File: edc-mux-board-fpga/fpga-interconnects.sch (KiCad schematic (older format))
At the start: 7 parts

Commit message: starting to work on mezzanine board interconnections.
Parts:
- added R?: 25Ω, symbol Device:R_Small_US
- added U?: 10CL040YF484I7G, SW-Intel:FBGA-484_23.0x23.0mm_Layout22x22_P1.0mm, symbol SW-Intel:10CL040YF484I7G
- added U?: S25FL128L, symbol SW-Cypress:S25FL128L
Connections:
- wire segments 0 -> 11
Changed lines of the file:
@@
 $Descr USLedger 17000 11000
 encoding utf-8
-Sheet 22 25
+Sheet 25 28
 Title ""
 Date ""
@@
 AR Path="/5CC3E5DC/5CE97E21" Ref="U?"  Part="4"
 AR Path="/5CC6CC1A/5CD304E3/5CE97E21" Ref="U?"  Part="4"
+AR Path="/5CB2F6E3/5CE97E21" Ref="U?"  Part="4"
 F 0 "U?" H 15600 7800 50  0000 L CNN
 F 1 "10CL040YF484I7G" H 15600 7700 50  0000 L CNN
@@
 Text Label 5400 2300 0    50   ~ 0
 DIN2
+$Comp
+L SW-Intel:10CL040YF484I7G U?
+U 3 1 5CB19AD5
+P 9400 6500
+F 0 "U?" H 10100 5300 50  0000 C CNN
+F 1 "10CL040YF484I7G" H 9000 7700 50  0000 C CNN
+F 2 "SW-Intel:FBGA-484_23.0x23.0mm_Layout22x22_P1.0mm" H 12100 7400 50  0001 C CNN
+F 3 "https://www.intel.com/content/www/us/en/programmable/products/fpga/cyclone-series/cyclone-10/cyclone-10-lp/support.html" H 12100 7400 50  0001 C CNN
+	3    9400 6500
+	1    0    0    -1
+$EndComp
+$Comp
+L SW-Cypress:S25FL128L U?
+U 1 1 5CB411F7
+P 7500 6300
+F 0 "U?" H 7700 6050 50  0000 C CNN
+F 1 "S25FL128L" H 7450 6550 50  0000 C CNN
+F 2 "" H 7500 6300 50  0001 C CNN
+F 3 "https://www.cypress.com/file/316171/download" H 7500 6300 50  0001 C CNN
+	1    7500 6300
+	-1   0    0    -1
+$EndComp
+Wire Wire Line
+	7950 6150 8050 6150
+Wire Wire Line
+	7950 6450 8450 6450
+Wire Wire Line
+	7950 6350 8450 6350
+Wire Wire Line
+	7950 6250 8450 6250
+$Comp
+L Device:R_Small_US R?
+U 1 1 5CB55A13
+P 8150 6150
+F 0 "R?" V 7900 6150 50  0000 C CNN
+F 1 "25Ω" V 8000 6150 50  0000 C CNN
+F 2 "" H 8150 6150 50  0001 C CNN
+F 3 "~" H 8150 6150 50  0001 C CNN
+	1    8150 6150
+	0    1    1    0
+$EndComp
+Wire Wire Line
+	8250 6150 8450 6150
+Wire Wire Line
+	8450 5400 8200 5400
+Wire Wire Line
+	8200 5400 8200 5000
+Wire Wire Line
+	8450 5500 8200 5500
+Wire Wire Line
+	8200 5500 8200 5400
+Connection ~ 8200 5400
+Wire Wire Line
+	8450 5700 8200 5700
+Wire Wire Line
+	8200 5700 8200 5500
+Connection ~ 8200 5500
 $EndSCHEMATC

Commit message: Finished CODEC and MCU interconnections
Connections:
- net labels added: SCL, SDA, ~RESET
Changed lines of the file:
@@
 	8200 5700 8200 5500
 Connection ~ 8200 5500
+Text HLabel 2050 8650 0    50   Input ~ 0
+~RESET
+Text HLabel 2350 7000 0    50   Input ~ 0
+SCL
+Text HLabel 2300 7200 0    50   BiDi ~ 0
+SDA
 $EndSCHEMATC

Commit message: Finished FPGA and MCU interconnections.
Finished up interrupt wiring
Fixed a few missing connections
Annotated Schematic
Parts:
- added C320: 100nF, symbol Device:C_Small
- added D4: CONF_STATUS (GREEN), symbol Device:LED
- added D5: CRC_ERR, symbol Device:LED
- added D6: CONF_ERR (RED), symbol Device:LED
- added J5: Conn_02x05_Counter_Clockwise, symbol Connector_Generic:Conn_02x05_Counter_Clockwise
- added JP1: LED_ENABLE, symbol Jumper:Jumper_2_Open
- added R123, R129, R130: 200Ω, symbol Device:R_Small_US
- added R124, R125, R126, R127, R128, R132, R133: 10kΩ, symbol Device:R_Small_US
- added R134: 1kΩ, symbol Device:R_Small_US
- added unit 6 of U1
- added unit 5 of U1
- gave numbers to parts that had none: 3
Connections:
- net labels added: +2V5, +3V3, ATTACH_INT_OUT, BCLK10, BCLK11, BCLK12, BCLK13, BCLK14, BCLK15, BCLK4, BCLK5, BCLK6, BCLK7, BCLK8, BCLK9, CLK0_FPGA, DEV_ATT0, DEV_ATT1, DEV_ATT10, DEV_ATT11, DEV_ATT12, DEV_ATT13, DEV_ATT14, DEV_ATT15, DEV_ATT2, DEV_ATT3, DEV_ATT4, DEV_ATT5, DEV_ATT6, DEV_ATT7, DEV_ATT8, DEV_ATT9, DEV_ATT[0..15], DEV_INT0, DEV_INT1, DEV_INT10, DEV_INT11, DEV_INT12, DEV_INT13, DEV_INT14, DEV_INT15, DEV_INT2, DEV_INT3, DEV_INT4, DEV_INT5, DEV_INT6, DEV_INT7, DEV_INT8, DEV_INT9, DEV_INT[0..15], DEV_INT_OUT0, DEV_INT_OUT1, DEV_INT_OUT2, DEV_INT_OUT3, DEV_INT_OUT4, DEV_INT_OUT5, DEV_INT_OUT6, DEV_INT_OUT7, DEV_INT_OUT[0..7], DIN10, DIN11, DIN12, DIN13, DIN14, DIN15, DIN4, DIN5, DIN6, DIN7, DIN8, DIN9, DOUT10, DOUT11, DOUT12, DOUT13, DOUT14, DOUT15, DOUT4, DOUT5, DOUT6, DOUT7, DOUT8, DOUT9, GND, LED_PWR, TCK, TDI, TDO, TMS, WCLK10, WCLK11, WCLK12, WCLK13, WCLK14, WCLK15, WCLK4, WCLK5, WCLK6, WCLK7, WCLK8, WCLK9
- wire segments 11 -> 221
- no-connect marks 0 -> 203
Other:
- note added: "CONF_STATUS: On before and during configuration\nCONF_ERR: On if configuration error"
- note added: "DIN = input to CODEC = i2s_out in VHDL\nDOUT = output from CODEC = i2s_in in VHDL"
- note added: "LED Forward Voltage of 2V:\n(3.3V - 2V)/200Ω = 6.5mA"
- moved on the sheet: R131, U1C, U1D, U1G, U1H, U1I, U1J, U1K, U1L, U58

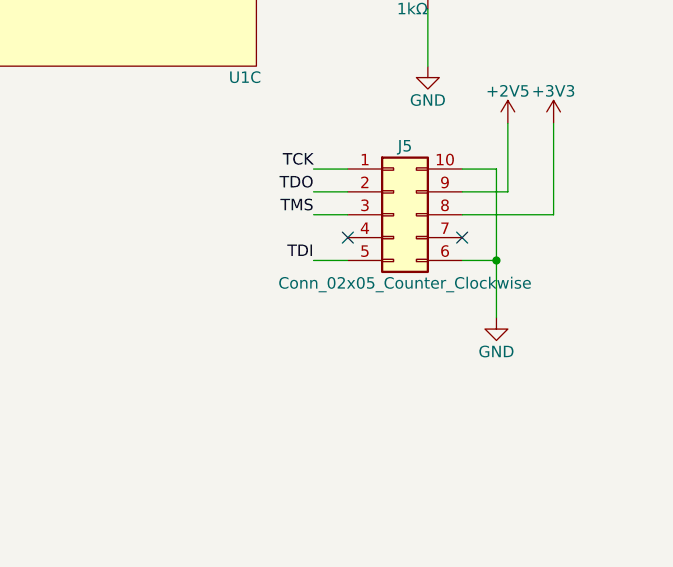
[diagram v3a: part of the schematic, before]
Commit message: assigned more footprints
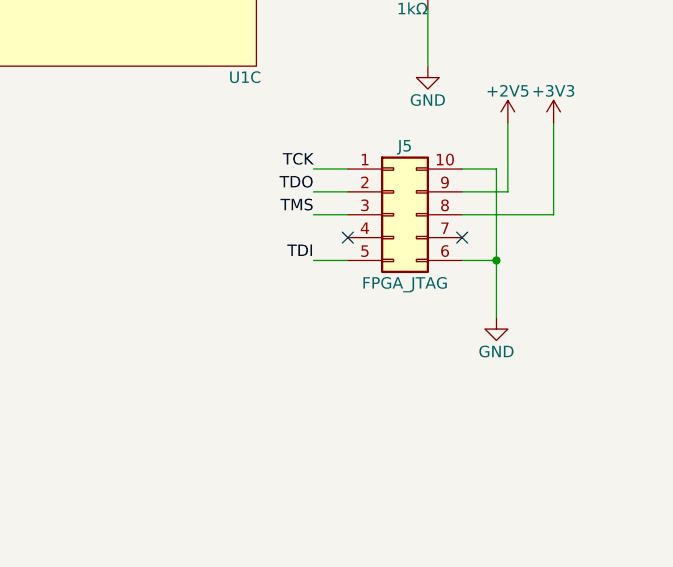
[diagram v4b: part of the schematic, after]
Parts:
- C320: footprint (none) -> Capacitor_SMD:C_0603_1608Metric; Package ID (none) -> 0603in/1608mm
- J5: value Conn_02x05_Counter_Clockwise -> FPGA_JTAG; footprint (none) -> Connector_PinHeader_1.27mm:PinHeader_2x05_P1.27mm_Vertical
- JP1: footprint (none) -> Connector_PinHeader_1.27mm:PinHeader_1x02_P1.27mm_Vertical
- R123, R124, R125, R126, R127, R128, R129, R130, R131, R132, R133, R134: footprint (none) -> Resistor_SMD:R_0402_1005Metric
- U58: footprint (none) -> Package_SON:WSON-8-1EP_6x5mm_P1.27mm_EP3.4x4mm
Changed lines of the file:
@@
 F 0 "U58" H 11750 4800 50  0000 C CNN
 F 1 "S25FL128L" H 11500 5300 50  0000 C CNN
-F 2 "" H 11550 5050 50  0001 C CNN
+F 2 "Package_SON:WSON-8-1EP_6x5mm_P1.27mm_EP3.4x4mm" H 11550 5050 50  0001 C CNN
 F 3 "https://www.cypress.com/file/316171/download" H 11550 5050 50  0001 C CNN
 	1    11550 5050
@@
 F 0 "R131" V 12000 4900 50  0000 C CNN
 F 1 "25Ω" V 12100 4900 50  0000 C CNN
-F 2 "" H 12250 4900 50  0001 C CNN
+F 2 "Resistor_SMD:R_0402_1005Metric" H 12250 4900 50  0001 C CNN
 F 3 "~" H 12250 4900 50  0001 C CNN
 	1    12250 4900
@@
 F 0 "C320" H 10850 5000 50  0000 R CNN
 F 1 "100nF" H 10850 5050 50  0000 R CNN
-F 2 "" H 10950 5050 50  0001 C CNN
+F 2 "Capacitor_SMD:C_0603_1608Metric" H 10950 5050 50  0001 C CNN
 F 3 "~" H 10950 5050 50  0001 C CNN
+F 4 "0603in/1608mm" H 0   0   50  0001 C CNN "Package ID"
 	1    10950 5050
 	1    0    0    1
@@
 F 0 "R125" V 15500 3850 50  0000 R CNN
 F 1 "10kΩ" V 15500 4200 50  0000 R CNN
-F 2 "" H 15450 3900 50  0001 C CNN
+F 2 "Resistor_SMD:R_0402_1005Metric" H 15450 3900 50  0001 C CNN
 F 3 "~" H 15450 3900 50  0001 C CNN
 	1    15450 3900
@@
 F 0 "R123" H 15150 3850 50  0000 L CNN
 F 1 "200Ω" H 15150 3900 50  0000 L CNN
-F 2 "" H 15050 3900 50  0001 C CNN
+F 2 "Resistor_SMD:R_0402_1005Metric" H 15050 3900 50  0001 C CNN
 F 3 "~" H 15050 3900 50  0001 C CNN
 	1    15050 3900
@@
 F 0 "R124" V 15350 3750 50  0000 L CNN
 F 1 "10kΩ" H 15300 4000 50  0000 L CNN
-F 2 "" H 15300 3900 50  0001 C CNN
+F 2 "Resistor_SMD:R_0402_1005Metric" H 15300 3900 50  0001 C CNN
 F 3 "~" H 15300 3900 50  0001 C CNN
 	1    15300 3900
@@
 F 0 "R126" V 15650 3850 50  0000 R CNN
 F 1 "10kΩ" V 15650 4200 50  0000 R CNN
-F 2 "" H 15600 3900 50  0001 C CNN
+F 2 "Resistor_SMD:R_0402_1005Metric" H 15600 3900 50  0001 C CNN
 F 3 "~" H 15600 3900 50  0001 C CNN
 	1    15600 3900
@@
 F 0 "R129" V 16100 3850 50  0000 R CNN
 F 1 "200Ω" V 16100 4200 50  0000 R CNN
-F 2 "" H 16050 3900 50  0001 C CNN
+F 2 "Resistor_SMD:R_0402_1005Metric" H 16050 3900 50  0001 C CNN
 F 3 "~" H 16050 3900 50  0001 C CNN
 	1    16050 3900
@@
 F 0 "JP1" V 15100 3000 50  0000 L CNN
 F 1 "LED_ENABLE" V 15050 3000 50  0000 L CNN
-F 2 "" H 15050 2900 50  0001 C CNN
+F 2 "Connector_PinHeader_1.27mm:PinHeader_1x02_P1.27mm_Vertical" H 15050 2900 50  0001 C CNN
 F 3 "~" H 15050 2900 50  0001 C CNN
 	1    15050 2900
@@
 F 0 "R134" V 15600 5900 50  0000 L CNN
 F 1 "1kΩ" H 15550 6150 50  0000 L CNN
-F 2 "" H 15550 6050 50  0001 C CNN
+F 2 "Resistor_SMD:R_0402_1005Metric" H 15550 6050 50  0001 C CNN
 F 3 "~" H 15550 6050 50  0001 C CNN
 	1    15550 6050
@@
 P 15400 7050
 F 0 "J5" H 15450 7350 50  0000 C CNN
-F 1 "Conn_02x05_Counter_Clockwise" H 15450 6750 50  0000 C CNN
-F 2 "" H 15400 7050 50  0001 C CNN
+F 1 "FPGA_JTAG" H 15450 6750 50  0000 C CNN
+F 2 "Connector_PinHeader_1.27mm:PinHeader_2x05_P1.27mm_Vertical" H 15400 7050 50  0001 C CNN
 F 3 "~" H 15400 7050 50  0001 C CNN
 	1    15400 7050
@@
 F 0 "R132" H 16100 5050 50  0000 L CNN
 F 1 "10kΩ" H 16100 5100 50  0000 L CNN
-F 2 "" H 16000 5100 50  0001 C CNN
+F 2 "Resistor_SMD:R_0402_1005Metric" H 16000 5100 50  0001 C CNN
 F 3 "~" H 16000 5100 50  0001 C CNN
 	1    16000 5100
@@
 F 0 "R133" H 16100 5050 50  0000 R CNN
 F 1 "10kΩ" H 16100 5100 50  0000 R CNN
-F 2 "" H 16200 5100 50  0001 C CNN
+F 2 "Resistor_SMD:R_0402_1005Metric" H 16200 5100 50  0001 C CNN
 F 3 "~" H 16200 5100 50  0001 C CNN
 	1    16200 5100
@@
 F 0 "R130" V 16200 4000 50  0000 L CNN
 F 1 "200Ω" V 16200 3600 50  0000 L CNN
-F 2 "" H 16250 3900 50  0001 C CNN
+F 2 "Resistor_SMD:R_0402_1005Metric" H 16250 3900 50  0001 C CNN
 F 3 "~" H 16250 3900 50  0001 C CNN
 	1    16250 3900
@@
 F 0 "R127" V 15800 3850 50  0000 R CNN
 F 1 "10kΩ" V 15800 4200 50  0000 R CNN
-F 2 "" H 15750 3900 50  0001 C CNN
+F 2 "Resistor_SMD:R_0402_1005Metric" H 15750 3900 50  0001 C CNN
 F 3 "~" H 15750 3900 50  0001 C CNN
 	1    15750 3900
@@
 F 0 "R128" V 15950 3850 50  0000 R CNN
 F 1 "10kΩ" V 15950 4200 50  0000 R CNN
-F 2 "" H 15900 3900 50  0001 C CNN
+F 2 "Resistor_SMD:R_0402_1005Metric" H 15900 3900 50  0001 C CNN
 F 3 "~" H 15900 3900 50  0001 C CNN
 	1    15900 3900
@@
 Wire Wire Line
 	12950 4350 13100 4350
+Connection ~ 12950 5500
 Wire Bus Line
 	7100 1450 7100 3500
-Connection ~ 12950 5500
 $EndSCHEMATC

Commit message: re-annotating after adding power ICs and decoupling capacitors.
Also verified most footprints, and updated schematic field data.
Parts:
- C431: renamed from C320; value 100nF -> 100nF X7R
- R123: renamed from R131; Package ID (none) -> 0402in/1005mm
- R124: renamed from R123; Package ID (none) -> 0402in/1005mm
- R125: renamed from R124; Package ID (none) -> 0402in/1005mm
- R126: renamed from R125; Package ID (none) -> 0402in/1005mm
- R127: renamed from R134; Package ID (none) -> 0402in/1005mm
- R128: renamed from R126; Package ID (none) -> 0402in/1005mm
- R129: renamed from R127; Package ID (none) -> 0402in/1005mm
- R130: renamed from R128; Package ID (none) -> 0402in/1005mm
- R131: renamed from R132; Package ID (none) -> 0402in/1005mm
- R132: renamed from R129; Package ID (none) -> 0402in/1005mm
- R133: Package ID (none) -> 0402in/1005mm
- R134: renamed from R130; Package ID (none) -> 0402in/1005mm
- U6: renamed from U1; Description (none) -> Intel Cyclone 10 LP FPGA; Manufacturer (none) -> Intel; Manufacturers Part Number (none) -> 10CL040YF484I7G; Package ID (none) -> 484BGA
- renumbered D6 to D4, D4 to D5, D5 to D6, U58 to U63

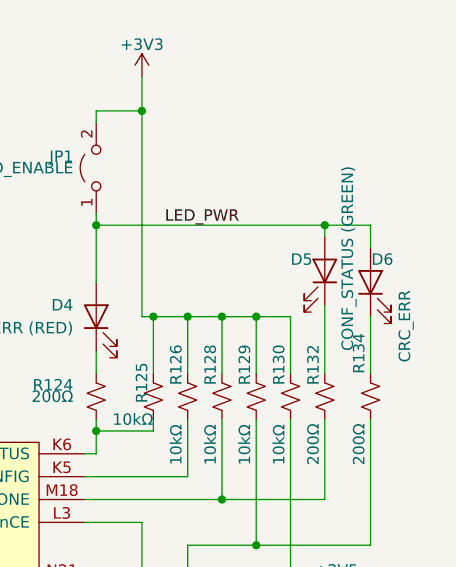
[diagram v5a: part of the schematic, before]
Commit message: Reannotating and adding more fields to components
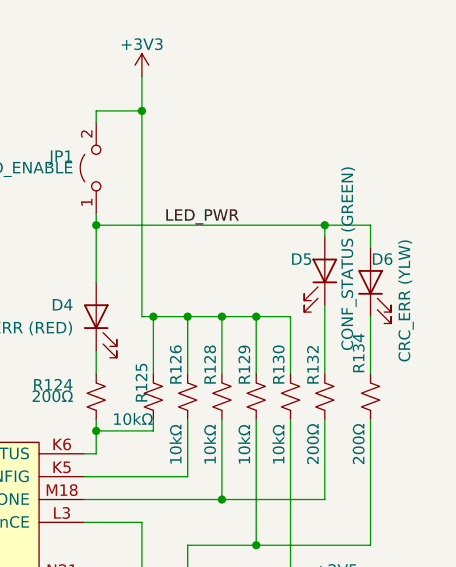
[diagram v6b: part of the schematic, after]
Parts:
- C431: Characteristics (none) -> CAP CER 0.1UF 25V X7R 0603; Description (none) -> MLCC Capacitor; Manufacturer (none) -> Kemet; Manufacturers Part Number (none) -> C0603C104J3RACAUTO
- D4: footprint (none) -> LED_SMD:LED_0402_1005Metric; Characteristics (none) -> Red; Description (none) -> Surface Mount LED Indicator; Manufacturer (none) -> SunLED; Manufacturers Part Number (none) -> XZMER68W-3; Package ID (none) -> 0402in/1005mm
- D5: footprint (none) -> LED_SMD:LED_0402_1005Metric; Characteristics (none) -> green; Description (none) -> Surface Mount LED Indicator; Manufacturer (none) -> SunLED; Manufacturers Part Number (none) -> XZVGR68W-3; Package ID (none) -> 0402in/1005mm
- D6: value CRC_ERR -> CRC_ERR (YLW); footprint (none) -> LED_SMD:LED_0402_1005Metric; Characteristics (none) -> Yellow; Description (none) -> Surface Mount LED Indicator; Manufacturer (none) -> SunLED; Manufacturers Part Number (none) -> XZMYK68W-2; Package ID (none) -> 0402in/1005mm
- J5: Description (none) -> FPGA JTAG Connector; Package ID (none) -> Through Hole
- JP1: Package ID (none) -> Through Hole
- R123, R124, R125, R126, R127, R128, R129, R130, R131, R132, R133, R134: Description (none) -> Resistor
- U63: Description (none) -> 256Mb flash memory for FPGA programming; Manufacturer (none) -> Cypress; Manufacturers Part Number (none) -> S25FL256L; Package ID (none) -> WSON8
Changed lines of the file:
@@
 F 2 "Package_SON:WSON-8-1EP_6x5mm_P1.27mm_EP3.4x4mm" H 11550 5050 50  0001 C CNN
 F 3 "https://www.cypress.com/file/316171/download" H 11550 5050 50  0001 C CNN
+F 4 "256Mb flash memory for FPGA programming" H 0   0   50  0001 C CNN "Description"
+F 5 "Cypress" H 0   0   50  0001 C CNN "Manufacturer"
+F 6 "S25FL256L" H 0   0   50  0001 C CNN "Manufacturers Part Number"
+F 7 "WSON8" H 0   0   50  0001 C CNN "Package ID"
 	1    11550 5050
 	-1   0    0    -1
@@
 F 3 "~" H 12250 4900 50  0001 C CNN
 F 4 "0402in/1005mm" H 0   0   50  0001 C CNN "Package ID"
+F 5 "Resistor" H 0   0   50  0001 C CNN "Description"
 	1    12250 4900
 	0    1    1    0
@@
 F 1 "100nF X7R" H 10850 5050 50  0000 R CNN
 F 2 "Capacitor_SMD:C_0603_1608Metric" H 10950 5050 50  0001 C CNN
-F 3 "~" H 10950 5050 50  0001 C CNN
+F 3 "https://content.kemet.com/datasheets/KEM_C1023_X7R_AUTO_SMD.pdf" H 10950 5050 50  0001 C CNN
 F 4 "0603in/1608mm" H 0   0   50  0001 C CNN "Package ID"
+F 5 "Kemet" H 0   0   50  0001 C CNN "Manufacturer"
+F 6 "C0603C104J3RACAUTO" H 0   0   50  0001 C CNN "Manufacturers Part Number"
+F 7 "CAP CER 0.1UF 25V X7R 0603" H 0   0   50  0001 C CNN "Characteristics"
+F 8 "MLCC Capacitor" H 0   0   50  0001 C CNN "Description"
 	1    10950 5050
 	1    0    0    1
@@
 F 3 "~" H 15450 3900 50  0001 C CNN
 F 4 "0402in/1005mm" H 0   0   50  0001 C CNN "Package ID"
+F 5 "Resistor" H 0   0   50  0001 C CNN "Description"
 	1    15450 3900
 	-1   0    0    1
@@
 F 0 "D4" V 15100 3650 50  0000 L CNN
 F 1 "CONF_ERR (RED)" V 15000 3650 50  0000 L CNN
-F 2 "" H 15050 3550 50  0001 C CNN
-F 3 "~" H 15050 3550 50  0001 C CNN
+F 2 "LED_SMD:LED_0402_1005Metric" H 15050 3550 50  0001 C CNN
+F 3 "https://www.sunledusa.com/products/spec/XZMER68W-3.pdf" H 15050 3550 50  0001 C CNN
+F 4 "Red" H 0   0   50  0001 C CNN "Characteristics"
+F 5 "Surface Mount LED Indicator" H 0   0   50  0001 C CNN "Description"
+F 6 "SunLED" H 0   0   50  0001 C CNN "Manufacturer"
+F 7 "XZMER68W-3" H 0   0   50  0001 C CNN "Manufacturers Part Number"
+F 8 "0402in/1005mm" H 0   0   50  0001 C CNN "Package ID"
 	1    15050 3550
 	0    -1   -1   0
@@
 F 3 "~" H 15050 3900 50  0001 C CNN
 F 4 "0402in/1005mm" H 0   0   50  0001 C CNN "Package ID"
+F 5 "Resistor" H 0   0   50  0001 C CNN "Description"
 	1    15050 3900
 	-1   0    0    1
@@
 F 3 "~" H 15300 3900 50  0001 C CNN
 F 4 "0402in/1005mm" H 0   0   50  0001 C CNN "Package ID"
+F 5 "Resistor" H 0   0   50  0001 C CNN "Description"
 	1    15300 3900
 	-1   0    0    1
@@
 F 3 "~" H 15600 3900 50  0001 C CNN
 F 4 "0402in/1005mm" H 0   0   50  0001 C CNN "Package ID"
+F 5 "Resistor" H 0   0   50  0001 C CNN "Description"
 	1    15600 3900
 	-1   0    0    1
@@
 F 0 "D5" V 16100 3200 50  0000 L CNN
 F 1 "CONF_STATUS (GREEN)" H 15700 3450 50  0000 L CNN
-F 2 "" H 16050 3350 50  0001 C CNN
-F 3 "~" H 16050 3350 50  0001 C CNN
+F 2 "LED_SMD:LED_0402_1005Metric" H 16050 3350 50  0001 C CNN
+F 3 "https://www.sunledusa.com/products/spec/XZVGR68W-3.pdf" H 16050 3350 50  0001 C CNN
+F 4 "green" H 0   0   50  0001 C CNN "Characteristics"
+F 5 "Surface Mount LED Indicator" H 0   0   50  0001 C CNN "Description"
+F 6 "SunLED" H 0   0   50  0001 C CNN "Manufacturer"
+F 7 "XZVGR68W-3" H 0   0   50  0001 C CNN "Manufacturers Part Number"
+F 8 "0402in/1005mm" H 0   0   50  0001 C CNN "Package ID"
 	1    16050 3350
 	0    1    -1   0
@@
 F 3 "~" H 16050 3900 50  0001 C CNN
 F 4 "0402in/1005mm" H 0   0   50  0001 C CNN "Package ID"
+F 5 "Resistor" H 0   0   50  0001 C CNN "Description"
 	1    16050 3900
 	-1   0    0    1
@@
 F 2 "Connector_PinHeader_1.27mm:PinHeader_1x02_P1.27mm_Vertical" H 15050 2900 50  0001 C CNN
 F 3 "~" H 15050 2900 50  0001 C CNN
+F 4 "Through Hole" H 0   0   50  0001 C CNN "Package ID"
 	1    15050 2900
 	0    -1   -1   0
@@
 F 3 "~" H 15550 6050 50  0001 C CNN
 F 4 "0402in/1005mm" H 0   0   50  0001 C CNN "Package ID"
+F 5 "Resistor" H 0   0   50  0001 C CNN "Description"
 	1    15550 6050
 	-1   0    0    1
@@
 F 2 "Connector_PinHeader_1.27mm:PinHeader_2x05_P1.27mm_Vertical" H 15400 7050 50  0001 C CNN
 F 3 "~" H 15400 7050 50  0001 C CNN
+F 4 "FPGA JTAG Connector" H 0   0   50  0001 C CNN "Description"
+F 5 "Through Hole" H 0   0   50  0001 C CNN "Package ID"
 	1    15400 7050
 	1    0    0    -1
@@
 F 3 "~" H 16000 5100 50  0001 C CNN
 F 4 "0402in/1005mm" H 0   0   50  0001 C CNN "Package ID"
+F 5 "Resistor" H 0   0   50  0001 C CNN "Description"
 	1    16000 5100
 	-1   0    0    1
@@
 F 3 "~" H 16200 5100 50  0001 C CNN
 F 4 "0402in/1005mm" H 0   0   50  0001 C CNN "Package ID"
+F 5 "Resistor" H 0   0   50  0001 C CNN "Description"
 	1    16200 5100
 	-1   0    0    1
@@
 P 16250 3400
 F 0 "D6" V 16350 3300 50  0000 L CNN
-F 1 "CRC_ERR" H 15900 3250 50  0000 L CNN
-F 2 "" H 16250 3400 50  0001 C CNN
-F 3 "~" H 16250 3400 50  0001 C CNN
+F 1 "CRC_ERR (YLW)" H 15900 3250 50  0000 L CNN
+F 2 "LED_SMD:LED_0402_1005Metric" H 16250 3400 50  0001 C CNN
+F 3 "https://www.sunledusa.com/products/spec/XZMYK68W-2.pdf" H 16250 3400 50  0001 C CNN
+F 4 "Yellow" H 0   0   50  0001 C CNN "Characteristics"
+F 5 "Surface Mount LED Indicator" H 0   0   50  0001 C CNN "Description"
+F 6 "SunLED" H 0   0   50  0001 C CNN "Manufacturer"
+F 7 "XZMYK68W-2" H 0   0   50  0001 C CNN "Manufacturers Part Number"
+F 8 "0402in/1005mm" H 0   0   50  0001 C CNN "Package ID"
 	1    16250 3400
 	0    -1   -1   0
@@
 F 3 "~" H 16250 3900 50  0001 C CNN
 F 4 "0402in/1005mm" H 0   0   50  0001 C CNN "Package ID"
+F 5 "Resistor" H 0   0   50  0001 C CNN "Description"
 	1    16250 3900
 	1    0    0    -1
@@
 F 3 "~" H 15750 3900 50  0001 C CNN
 F 4 "0402in/1005mm" H 0   0   50  0001 C CNN "Package ID"
+F 5 "Resistor" H 0   0   50  0001 C CNN "Description"
 	1    15750 3900
 	-1   0    0    1
@@
 F 3 "~" H 15900 3900 50  0001 C CNN
 F 4 "0402in/1005mm" H 0   0   50  0001 C CNN "Package ID"
+F 5 "Resistor" H 0   0   50  0001 C CNN "Description"
 	1    15900 3900
 	-1   0    0    1
